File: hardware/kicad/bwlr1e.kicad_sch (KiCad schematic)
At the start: 62 parts, among them J1 Qwiic, Q1 AO3407, Q2 DMG1012UW, SW3 RESET, SW4 BOOT, U1 BME688, U2 RAK3172, U3 AEM10941-QFN, U4 XC6215

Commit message: fix led polarity and minor wiring changes
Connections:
- net +3V3: no longer R12.1, R13.1
- net GND: now also R12.1, R13.1
- net LED2: now also U2.6 (PA1); no longer U2.4 (UART1_TX/PB6)
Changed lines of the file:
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@@
   (junction (at 217.17 53.34) (diameter 0) (color 0 0 0 0)
   )
+  (junction (at 300.355 170.815) (diameter 0) (color 0 0 0 0)
+  )
   (junction (at 182.245 114.3) (diameter 0) (color 0 0 0 0)
   )
@@
   )
   (junction (at 366.395 116.84) (diameter 0) (color 0 0 0 0)
-  )
-  (junction (at 300.355 164.465) (diameter 0) (color 0 0 0 0)
   )
   (junction (at 194.945 114.3) (diameter 0) (color 0 0 0 0)
@@
   (no_connect (at 118.11 157.48))
   (no_connect (at 260.35 43.18))
-  (no_connect (at 118.11 152.4))
+  (no_connect (at 67.31 149.86))
   (no_connect (at 67.31 147.32))
   (no_connect (at 67.31 154.94))
@@
     (stroke (width 0) (type default))
   )
+  (wire (pts (xy 300.355 170.815) (xy 300.355 174.625))
+    (stroke (width 0) (type default))
+  )
   (wire (pts (xy 260.35 27.94) (xy 278.13 27.94))
     (stroke (width 0) (type default))
@@
     (stroke (width 0) (type default))
   )
+  (wire (pts (xy 300.355 164.465) (xy 300.355 170.815))
+    (stroke (width 0) (type default))
+  )
   (wire (pts (xy 48.26 119.38) (xy 48.26 124.46))
     (stroke (width 0) (type default))
@@
     (stroke (width 0) (type default))
   )
-  (wire (pts (xy 300.355 164.465) (xy 300.355 170.815))
-    (stroke (width 0) (type default))
-  )
   (wire (pts (xy 118.11 124.46) (xy 130.81 124.46))
     (stroke (width 0) (type default))
@@
     (stroke (width 0) (type default))
   )
-  (wire (pts (xy 67.31 149.86) (xy 60.96 149.86))
+  (wire (pts (xy 67.31 142.24) (xy 60.96 142.24))
     (stroke (width 0) (type default))
   )
@@
     (stroke (width 0) (type default))
   )
-  (wire (pts (xy 67.31 142.24) (xy 60.96 142.24))
+  (wire (pts (xy 124.46 152.4) (xy 118.11 152.4))
     (stroke (width 0) (type default))
   )
@@
   )
   (polyline (pts (xy 127 50.8) (xy 161.925 50.8))
-    (stroke (width 0) (type default))
-  )
-  (wire (pts (xy 300.355 159.385) (xy 300.355 164.465))
     (stroke (width 0) (type default))
   )
@@
     (effects (font (size 1.27 1.27)) (justify right bottom))
   )
-  (label "LED2" (at 60.96 149.86 0) (fields_autoplaced)
-    (effects (font (size 1.27 1.27)) (justify left bottom))
+  (label "LED2" (at 124.46 152.4 180) (fields_autoplaced)
+    (effects (font (size 1.27 1.27)) (justify right bottom))
   )
   (label "RST" (at 60.96 119.38 0) (fields_autoplaced)
@@
     )
   )
-  (symbol (lib_id "power:+3V3") (at 300.355 159.385 0) (mirror y) (unit 1)
-    (in_bom yes) (on_board yes) (dnp no)
-    (property "Reference" "#PWR0130" (at 300.355 163.195 0)
-      (effects (font (size 1.27 1.27)) hide)
-    )
-    (property "Value" "+3V3" (at 297.815 155.575 0)
-      (effects (font (size 1.27 1.27)) (justify right))
-    )
-    (property "Footprint" "" (at 300.355 159.385 0)
-      (effects (font (size 1.27 1.27)) hide)
-    )
-    (property "Datasheet" "" (at 300.355 159.385 0)
-      (effects (font (size 1.27 1.27)) hide)
-    )
-    (pin "1")
-    (instances
-      (project "bwlr1e"
-        (path "/630c8da6-5464-4eef-824d-89618087f4b4"
-          (reference "#PWR0130") (unit 1)
-        )
-      )
-    )
-  )
   (symbol (lib_id "Sensor:BME680") (at 368.935 135.89 0) (unit 1)
     (in_bom yes) (on_board yes) (dnp no) (fields_autoplaced)
@@
         )
       )
+    )
+  )
+  (symbol (lib_id "power:GND") (at 300.355 174.625 0) (unit 1)
+    (in_bom yes) (on_board yes) (dnp no) (fields_autoplaced)
+    (property "Reference" "#PWR010" (at 300.355 180.975 0)
+      (effects (font (size 1.27 1.27)) hide)
+    )
+    (property "Value" "GND" (at 300.355 179.705 0)
+      (effects (font (size 1.27 1.27)))
+    )
+    (property "Footprint" "" (at 300.355 174.625 0)
+      (effects (font (size 1.27 1.27)) hide)
+    )
+    (property "Datasheet" "" (at 300.355 174.625 0)
+      (effects (font (size 1.27 1.27)) hide)
+    )
+    (pin "1")
+    (instances
+      (project "bwlr1e"
+        (path "/630c8da6-5464-4eef-824d-89618087f4b4"
+          (reference "#PWR010") (unit 1)
+        )
+      )

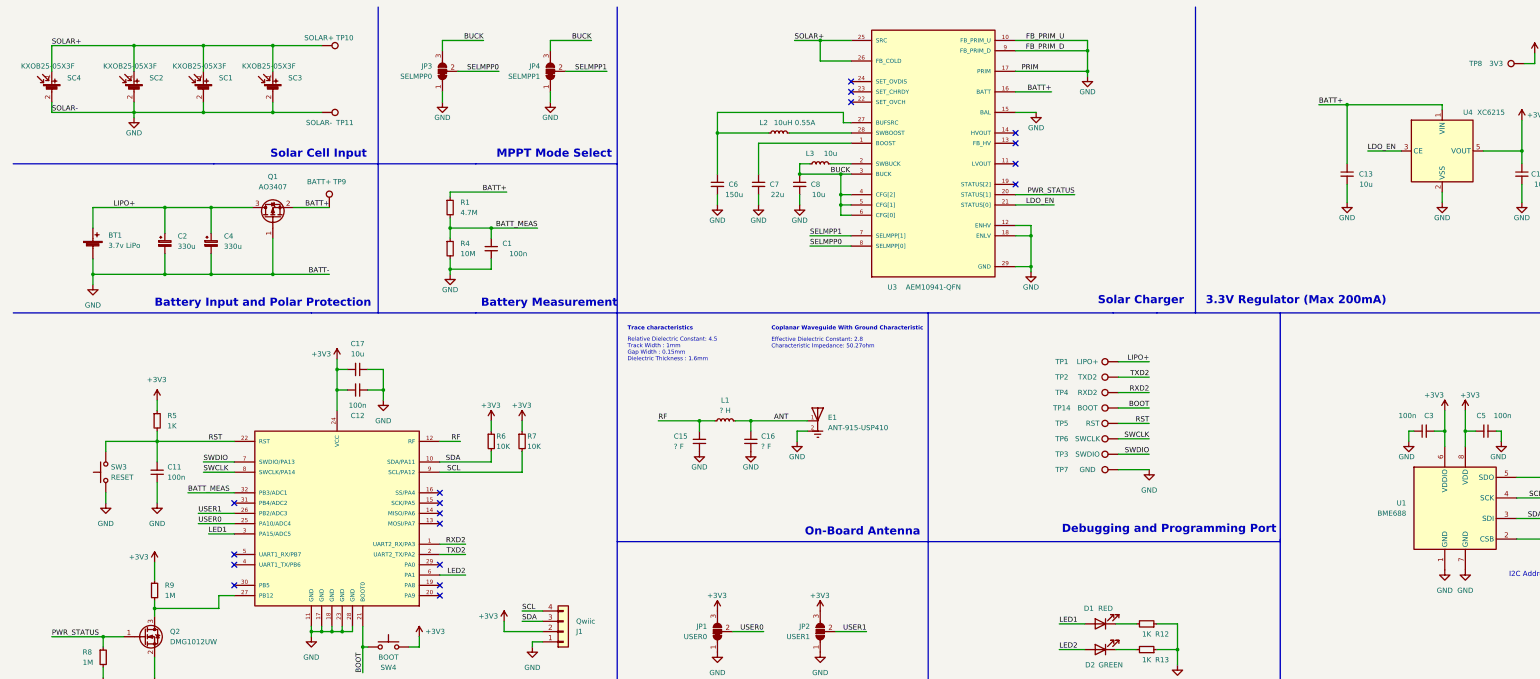
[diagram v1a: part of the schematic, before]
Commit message: change library to project-level and minor changes
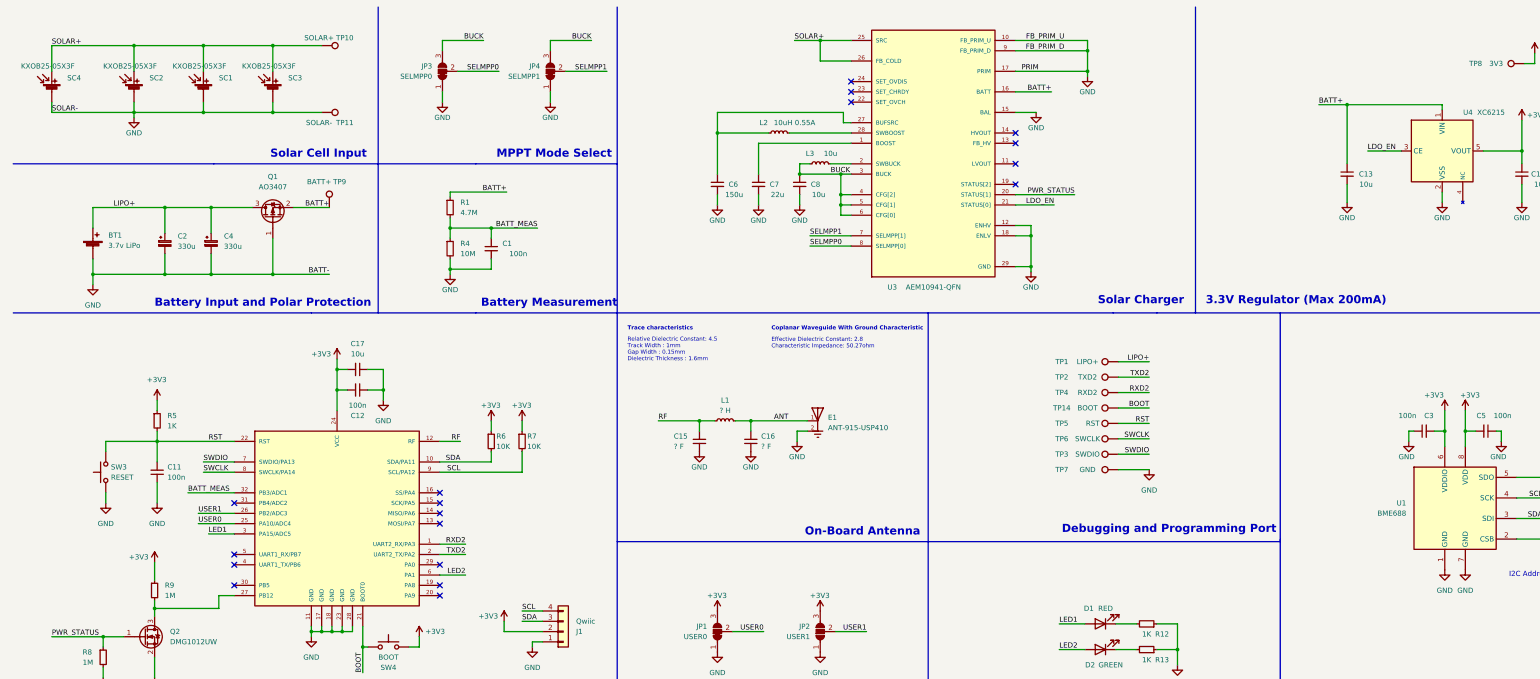
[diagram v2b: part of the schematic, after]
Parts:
- BT1: footprint Connector_JST:JST_PH_S2B-PH-SM4-TB_1x02-1MP_P2.00mm_Horizontal -> bwlr1e:JST_PH_S2B-PH-SM4-TB_1x02-1MP_P2.00mm_Horizontal
- E1: footprint XDCR_ANT-915-USP410 -> bwlr1e:XDCR_ANT-915-USP410; symbol Teapot:ANT-915-USP410 -> bwlr1e:ANT-915-USP410; MANUFACTURER Linx -> (none); MAXIMUM_PACKAGE_HEIGHT 2.9 mm -> (none); PARTREV N/A -> (none); STANDARD Manufacturer Recommendations -> (none)
- J1: footprint Connector_JST:JST_SH_SM04B-SRSS-TB_1x04-1MP_P1.00mm_Horizontal -> bwlr1e:JST_SH_SM04B-SRSS-TB_1x04-1MP_P1.00mm_Horizontal
- L2: footprint Teapot:IND_LPS4012-103MRB -> bwlr1e:IND_LPS4012-103MRB
- SC1, SC2, SC3, SC4: footprint Teapot:KXOB25-05X3F -> bwlr1e:KXOB25-05X3F
- U1: footprint Teapot:BME680-PSON80P300X300X100-8N -> bwlr1e:BME680-PSON80P300X300X100-8N
- U2: footprint Teapot:RAK3172 -> bwlr1e:RAK3172; symbol Teapot:RAK3172 -> bwlr1e:RAK3172
- U3: symbol Teapot:AEM10941-QFN -> bwlr1e:AEM10941-QFN
- U4: symbol Teapot:XC6220 -> bwlr1e:XC6220
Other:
- title: Teapot BWLR1E -> Teapotlabs BWLR1E
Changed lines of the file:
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@@
   (paper "User" 424.993 240.995)
   (title_block
-    (title "Teapot BWLR1E")
-    (date "2022-10-22")
+    (title "Teapotlabs BWLR1E")
+    (date "2023-08-12")
     (rev "4")
     (company "Teapot Laboratories")
@@
     (effects (font (size 1.27 1.27)) (justify right bottom))
   )
-  (symbol (lib_id "Teapot:RAK3172") (at 92.71 138.43 0) (unit 1)
+  (symbol (lib_id "bwlr1e:RAK3172") (at 92.71 138.43 0) (unit 1)
     (in_bom yes) (on_board yes) (dnp no) (fields_autoplaced)
     (property "Reference" "U2" (at 72.39 162.56 0)
@@
       (effects (font (size 1.27 1.27)) (justify left bottom) hide)
     )
-    (property "Footprint" "Teapot:RAK3172" (at 67.31 170.18 0)
+    (property "Footprint" "bwlr1e:RAK3172" (at 67.31 170.18 0)
       (effects (font (size 1.27 1.27)) (justify left bottom) hide)
     )
@@
       (effects (font (size 1.27 1.27)) (justify left))
     )
-    (property "Footprint" "Connector_JST:JST_SH_SM04B-SRSS-TB_1x04-1MP_P1.00mm_Horizontal" (at 148.59 166.37 0)
+    (property "Footprint" "bwlr1e:JST_SH_SM04B-SRSS-TB_1x04-1MP_P1.00mm_Horizontal" (at 148.59 166.37 0)
       (effects (font (size 1.27 1.27)) hide)
     )
@@
       (effects (font (size 1.27 1.27)) (justify right))
     )
-    (property "Footprint" "Teapot:BME680-PSON80P300X300X100-8N" (at 405.765 147.32 0)
+    (property "Footprint" "bwlr1e:BME680-PSON80P300X300X100-8N" (at 405.765 147.32 0)
       (effects (font (size 1.27 1.27)) hide)
     )
@@
     )
   )
-  (symbol (lib_id "Teapot:XC6220") (at 365.76 40.005 0) (unit 1)
+  (symbol (lib_id "bwlr1e:XC6220") (at 365.76 40.005 0) (unit 1)
     (in_bom yes) (on_board yes) (dnp no)
     (property "Reference" "U4" (at 372.11 38.1 0)
@@
       (effects (font (size 1.27 1.27)) hide)
     )
-    (property "Datasheet" "https://www.mouser.com/datasheet/2/760/TOSL_S_A0009829727_1-2575077.pdf" (at 365.76 71.755 0)
+    (property "Datasheet" "https://www.torexsemi.com/file/xc6220/XC6220.pdf" (at 365.76 71.755 0)
       (effects (font (size 1.27 1.27)) hide)
     )
+    (pin "4")
     (pin "1")
     (pin "2")
@@
     )
   )
-  (symbol (lib_name "Solar_Cell_1") (lib_id "Device:Solar_Cell") (at 76.835 33.02 0) (unit 1)
+  (symbol (lib_id "Device:Solar_Cell") (at 76.835 33.02 0) (unit 1)
     (in_bom yes) (on_board yes) (dnp no)
     (property "Reference" "SC3" (at 80.645 29.5909 0)
@@
       (effects (font (size 1.27 1.27)) (justify left))
     )
-    (property "Footprint" "Teapot:KXOB25-05X3F" (at 76.835 31.496 90)
+    (property "Footprint" "bwlr1e:KXOB25-05X3F" (at 76.835 31.496 90)
       (effects (font (size 1.27 1.27)) hide)
     )
@@
     )
   )
-  (symbol (lib_name "Solar_Cell_1") (lib_id "Device:Solar_Cell") (at 59.69 33.02 0) (unit 1)
+  (symbol (lib_id "Device:Solar_Cell") (at 59.69 33.02 0) (unit 1)
     (in_bom yes) (on_board yes) (dnp no)
     (property "Reference" "SC1" (at 63.5 29.5909 0)
@@
       (effects (font (size 1.27 1.27)) (justify left))
     )
-    (property "Footprint" "Teapot:KXOB25-05X3F" (at 59.69 31.496 90)
+    (property "Footprint" "bwlr1e:KXOB25-05X3F" (at 59.69 31.496 90)
       (effects (font (size 1.27 1.27)) hide)
     )
@@
     )
   )
-  (symbol (lib_id "Teapot:ANT-915-USP410") (at 211.455 114.3 0) (unit 1)
+  (symbol (lib_id "bwlr1e:ANT-915-USP410") (at 211.455 114.3 0) (unit 1)
     (in_bom yes) (on_board yes) (dnp no)
     (property "Reference" "E1" (at 213.995 113.4744 0)
@@
       (effects (font (size 1.27 1.27)) (justify left))
     )
-    (property "Footprint" "XDCR_ANT-915-USP410" (at 206.375 124.46 0)
+    (property "Footprint" "bwlr1e:XDCR_ANT-915-USP410" (at 206.375 124.46 0)
       (effects (font (size 1.27 1.27)) (justify left bottom) hide)
     )
@@
       (effects (font (size 1.27 1.27)) (justify left bottom) hide)
     )
-    (property "MAXIMUM_PACKAGE_HEIGHT" "2.9 mm" (at 213.995 109.22 0)
-      (effects (font (size 1.27 1.27)) (justify left bottom) hide)
-    )
-    (property "MANUFACTURER" "Linx" (at 210.185 110.49 0)
-      (effects (font (size 1.27 1.27)) (justify left bottom) hide)
-    )
-    (property "PARTREV" "N/A" (at 203.835 109.22 0)
-      (effects (font (size 1.27 1.27)) (justify left bottom) hide)
-    )
-    (property "STANDARD" "Manufacturer Recommendations" (at 208.915 121.92 0)
-      (effects (font (size 1.27 1.27)) (justify left bottom) hide)
-    )
     (pin "1")
     (pin "2")
@@
       (effects (font (size 1.27 1.27)))
     )
-    (property "Footprint" "Teapot:IND_LPS4012-103MRB" (at 201.93 43.18 0)
+    (property "Footprint" "bwlr1e:IND_LPS4012-103MRB" (at 201.93 43.18 0)
       (effects (font (size 1.27 1.27)) hide)
     )
-    (property "Datasheet" "https://www.mouser.com/datasheet/2/597/lps4012-1890589.pdf" (at 201.93 43.18 0)
+    (property "Datasheet" "~" (at 201.93 43.18 0)
       (effects (font (size 1.27 1.27)) hide)
     )
@@
       (effects (font (size 1.27 1.27)) (justify left))
     )
-    (property "Footprint" "Connector_JST:JST_PH_S2B-PH-SM4-TB_1x02-1MP_P2.00mm_Horizontal" (at 32.385 70.231 90)
+    (property "Footprint" "bwlr1e:JST_PH_S2B-PH-SM4-TB_1x02-1MP_P2.00mm_Horizontal" (at 32.385 70.231 90)
       (effects (font (size 1.27 1.27)) hide)
     )
@@
     )
   )
-  (symbol (lib_name "Solar_Cell_1") (lib_id "Device:Solar_Cell") (at 42.545 33.02 0) (unit 1)
+  (symbol (lib_id "Device:Solar_Cell") (at 42.545 33.02 0) (unit 1)
     (in_bom yes) (on_board yes) (dnp no)
     (property "Reference" "SC2" (at 46.355 29.5909 0)
@@
       (effects (font (size 1.27 1.27)) (justify left))
     )
-    (property "Footprint" "Teapot:KXOB25-05X3F" (at 42.545 31.496 90)
+    (property "Footprint" "bwlr1e:KXOB25-05X3F" (at 42.545 31.496 90)
       (effects (font (size 1.27 1.27)) hide)
     )
@@
     )
   )
-  (symbol (lib_name "Solar_Cell_1") (lib_id "Device:Solar_Cell") (at 22.225 33.02 0) (unit 1)
+  (symbol (lib_id "Device:Solar_Cell") (at 22.225 33.02 0) (unit 1)
     (in_bom yes) (on_board yes) (dnp no)
     (property "Reference" "SC4" (at 26.035 29.5909 0)
@@
       (effects (font (size 1.27 1.27)) (justify left))
     )
-    (property "Footprint" "Teapot:KXOB25-05X3F" (at 22.225 31.496 90)
+    (property "Footprint" "bwlr1e:KXOB25-05X3F" (at 22.225 31.496 90)
       (effects (font (size 1.27 1.27)) hide)
     )
@@
     )
   )
-  (symbol (lib_id "Teapot:AEM10941-QFN") (at 240.03 48.26 0) (unit 1)
+  (symbol (lib_id "bwlr1e:AEM10941-QFN") (at 240.03 48.26 0) (unit 1)
     (in_bom yes) (on_board yes) (dnp no)
     (property "Reference" "U3" (at 229.87 81.28 0)
